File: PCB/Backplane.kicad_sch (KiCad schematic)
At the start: 123 parts, among them J1 L_XLR_In, J10 R_Pre_Out, J11 TRS_Out, J12 RCA_Pre_Out, J13 DD21.0121.1111, J14 ICSP, J2 R_XLR_In, J3 RCA_In, J8 XLR_Out, J9 L_Pre_Out, K1 G6K-2, K2 G6K-2, K3 G6K-2, K4 G6K-2, K5 G6K-2, K6 G6K-2, K7 G6K-2, K8 G5LE-1, SW1 Reset, SW2 Input mode, SW3 Standby, SW4 Output mode, U1 LM339, U10 ATtiny2313A-P, U11 ULN2803A, U12 MC7812ACTG, U13 MC7912ACTG, U14 Attenuator, U2 LM339, U3 Attenuator, U4 Amp_Module, U5 Amp_Module, U6 Amp_Module, U7 Amp_Module, U8 74LS02, U9 LM393, Y1 16M

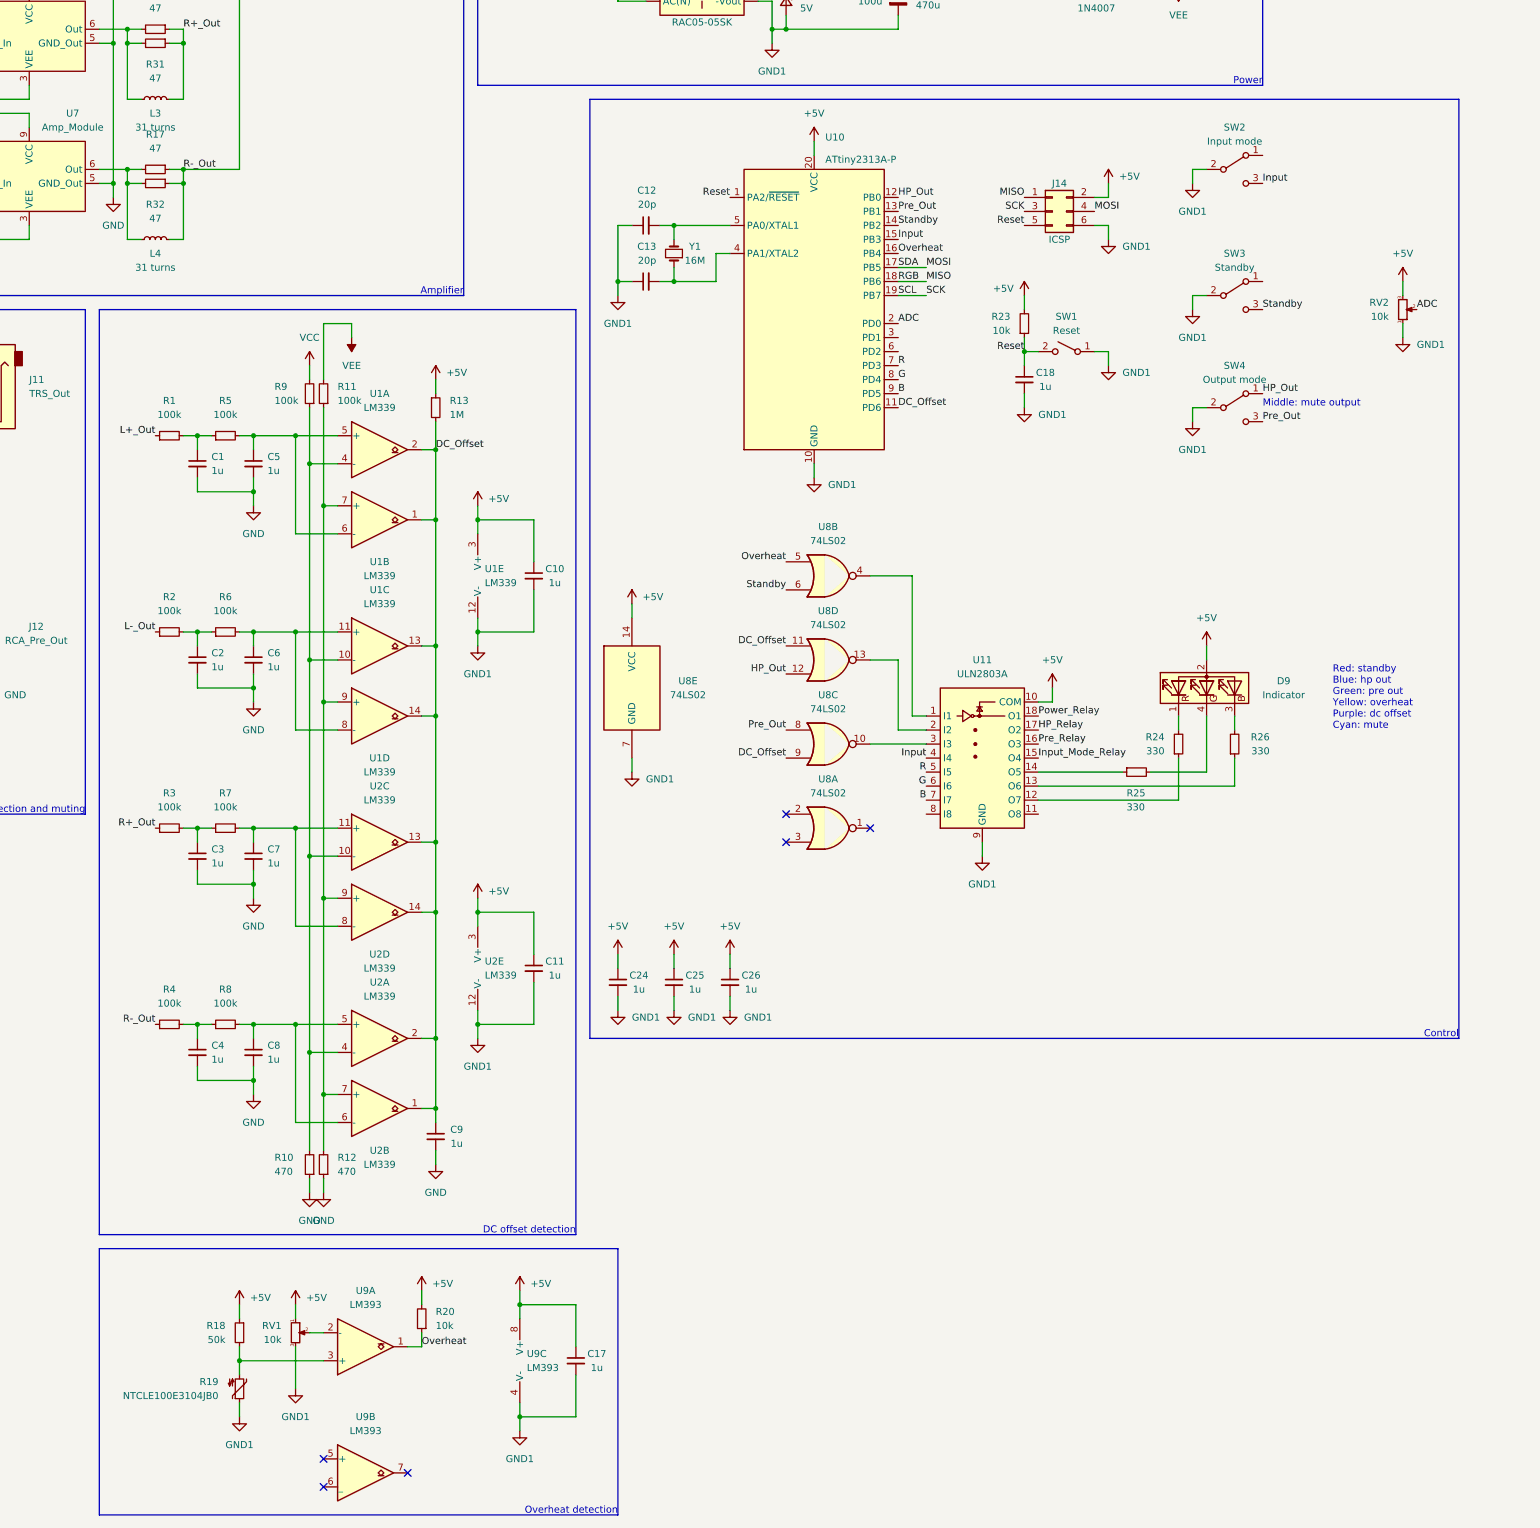
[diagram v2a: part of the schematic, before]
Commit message: Added bulk capacitance to each IC, rerouted 5V line on backplane board
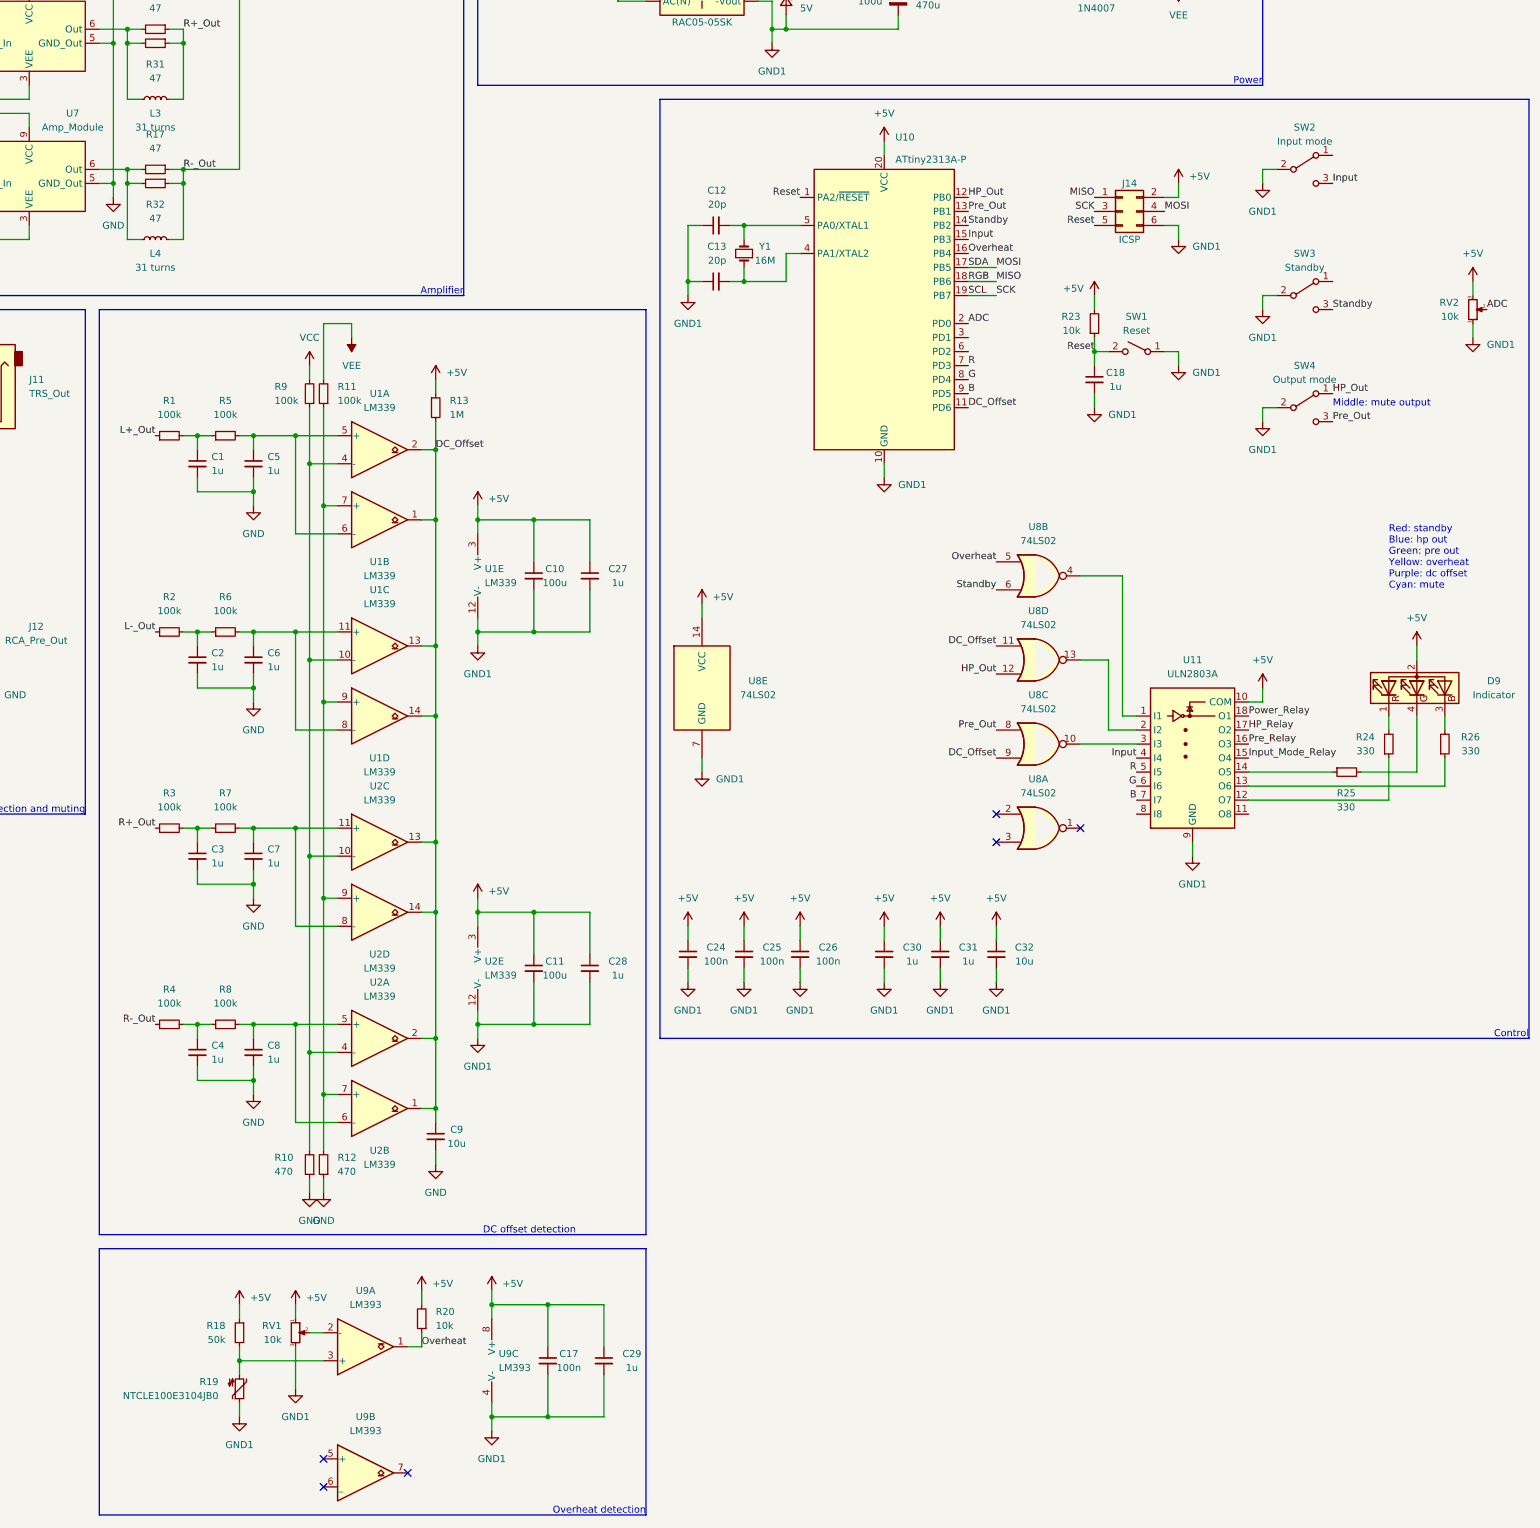
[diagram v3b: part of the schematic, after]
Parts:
- added C27, C28, C29, C30, C31: 1u, Capacitor_SMD:C_0603_1608Metric, symbol Device:C_Small
- added C32: 10u, Capacitor_SMD:C_0603_1608Metric, symbol Device:C_Small
- C10, C11: value 1u -> 100u
- C17, C24, C25, C26: value 1u -> 100n
- C9: value 1u -> 10u
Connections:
- net +5V: now also C27.1, C28.1, C29.1, C30.1, C31.1, C32.1
- net GND1: now also C27.2, C28.2, C29.2, C30.2, C31.2, C32.2
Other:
- moved on the sheet: C12, C13, C17, C18, C24, C25, C26, D9, J14, R23, R24, R25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
